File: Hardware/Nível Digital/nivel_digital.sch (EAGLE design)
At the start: 9 parts

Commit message: Botão range adicionado
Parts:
- added S4: (no value), GEAP:10-XXPUSH-BUTTON-5MM
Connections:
- new net HOLD: S3.S, S3.S1
- new net N$1: U$1.SCL
- new net N$2: U$1.SDA
- new net RANGE: S4.S, S4.S1
- new net ZERO: S2.S, S2.S1
- net +3V3: now also U$2.VCC
- net +5V: now also U$1.VCC
- net GND: now also S2.P, S2.P1, S3.P, S3.P1, S4.P, S4.P1, U$1.GND, U$2.GND
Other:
- note removed: "HOLD"
- note removed: "ZERO"
- moved on the sheet: AD, IOH, IOL, POWER, S1, S2, S3, U$1, U$2

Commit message: Botao Range + pinagem dos botões
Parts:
- removed S1: (no value), GEAP:10-XXPUSH-BUTTON-5MM
- removed U$1: (no value), GEAP:OLED_0.96_I2C
- removed U$2: MODULO_ADXL345, GEAP:MODULO_ADXL345
- added DS1: (no value), GEAP:OLED_0.96_I2C
- added IC1: MODULO_ADXL345, GEAP:MODULO_ADXL345
- added R1, R2: (no value), rcl:R-US_0204/7
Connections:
- removed net HOLD: S3.S, S3.S1
- removed net N$1: U$1.SCL
- removed net N$2: U$1.SDA
- removed net RANGE: S4.S, S4.S1
- removed net ZERO: S2.S, S2.S1
- net +3V3: now also IC1.3.3V; no longer U$2.VCC
- net +5V: now also DS1.VCC; no longer U$1.VCC
- net AD0: now also R1.1, R2.2
- net AD4/SDA: now also DS1.SDA, IC1.SDA
- net AD5/SCL: now also DS1.SCL, IC1.SCL
- net GND: now also DS1.GND, IC1.GND, R2.1; no longer S1.P, S1.P1, U$1.GND, U$2.GND
- net IO5: now also S2.S, S2.S1
- net IO6: now also S3.S, S3.S1
- net IO7: now also S4.S, S4.S1
- net RESET: no longer S1.S, S1.S1
- net VIN: now also R1.2
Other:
- note added: "HOLD"
- note added: "RANGE"
- note added: "ZERO"
- moved on the sheet: S2, S3, S4

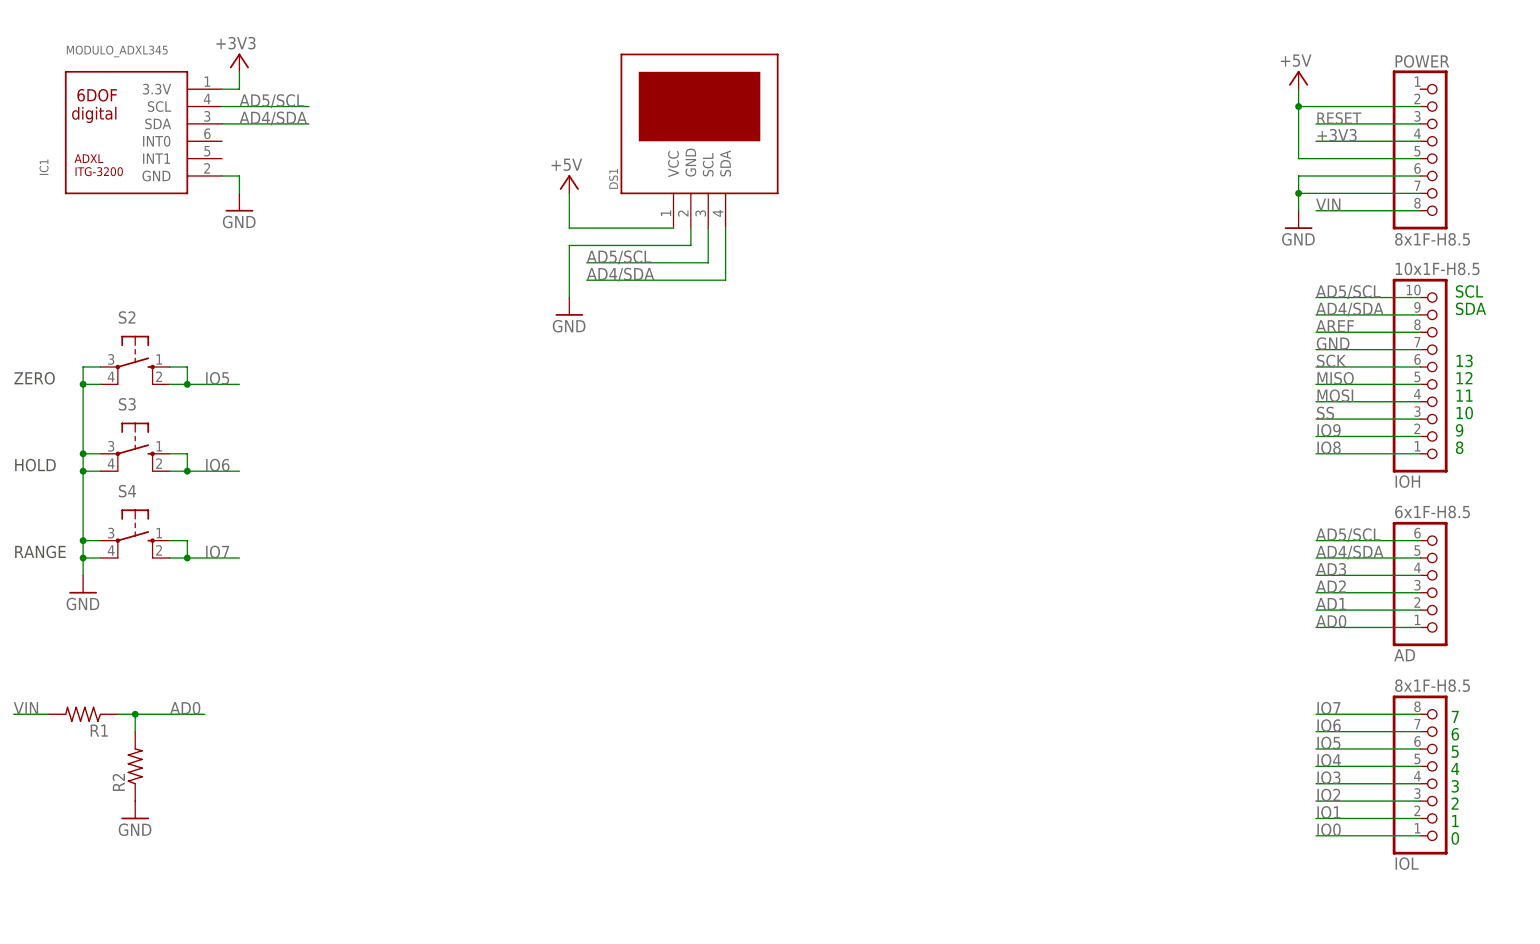
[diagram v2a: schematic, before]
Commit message: Display e acelerômetro novos
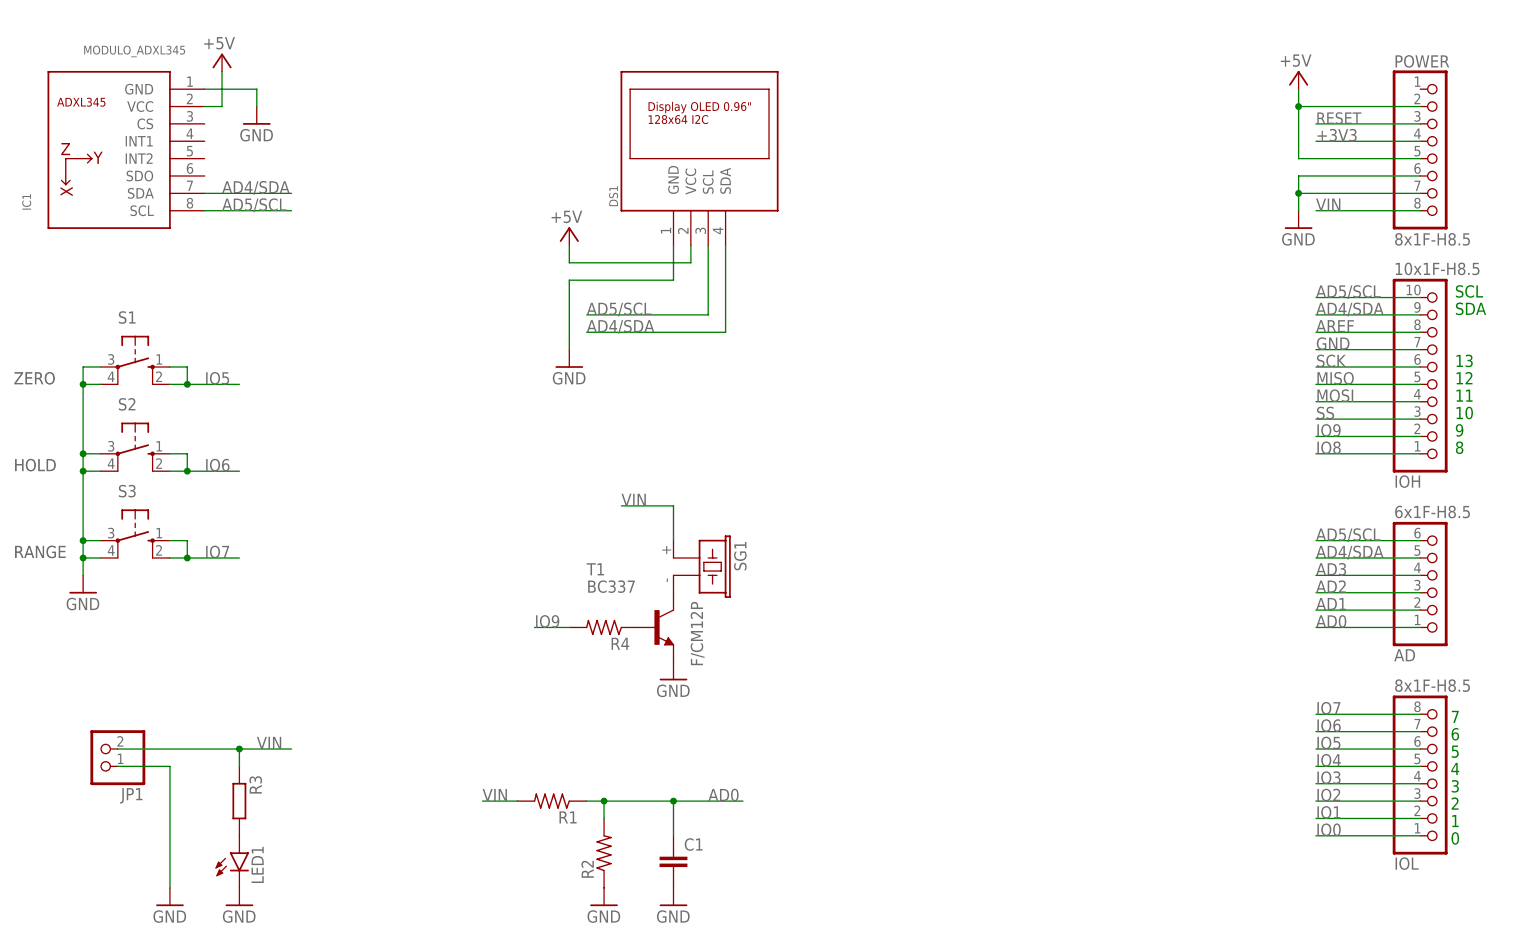
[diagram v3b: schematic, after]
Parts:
- removed S4: (no value), GEAP:10-XXPUSH-BUTTON-5MM
- added C1: (no value), rcl:C-EU050-025X075
- added JP1: (no value), pinhead:PINHD-1X2/90
- added LED1: (no value), led:LED5MM
- added R3: (no value), rcl:R-EU_0207/10
- added R4: (no value), rcl:R-US_0204/7
- added S1: (no value), GEAP:10-XXPUSH-BUTTON-5MM
- added SG1: F/CM12P, buzzer:F/CM12P
- added T1: BC337, transistor:BC337
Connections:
- new net N$1: LED1.A, R3.2
- new net N$2: SG1.2, T1.C
- new net N$3: R4.1, T1.B
- net +3V3: no longer IC1.3.3V
- net +5V: now also IC1.VCC
- net AD0: now also C1.1
- net GND: now also C1.2, JP1.1, LED1.C, S1.P, S1.P1, T1.E; no longer S4.P, S4.P1
- net IO5: now also S1.S, S1.S1; no longer S2.S, S2.S1
- net IO6: now also S2.S, S2.S1; no longer S3.S, S3.S1
- net IO7: now also S3.S, S3.S1; no longer S4.S, S4.S1
- net IO9: now also R4.2
- net VIN: now also JP1.2, R3.1, SG1.1
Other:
- moved on the sheet: R1, R2, S2, S3
